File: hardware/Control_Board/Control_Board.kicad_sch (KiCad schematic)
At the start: 22 parts, among them J1 Left Motor, J2 Right Motor, J3 Battery, J4 MPU-6050, J5 Pitch Motor, Q1 2N3904, Q2 2N3904, Q4 2N3904, SW1 Extra_BTN, U1 ESP32-FREENOVE-WROVER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

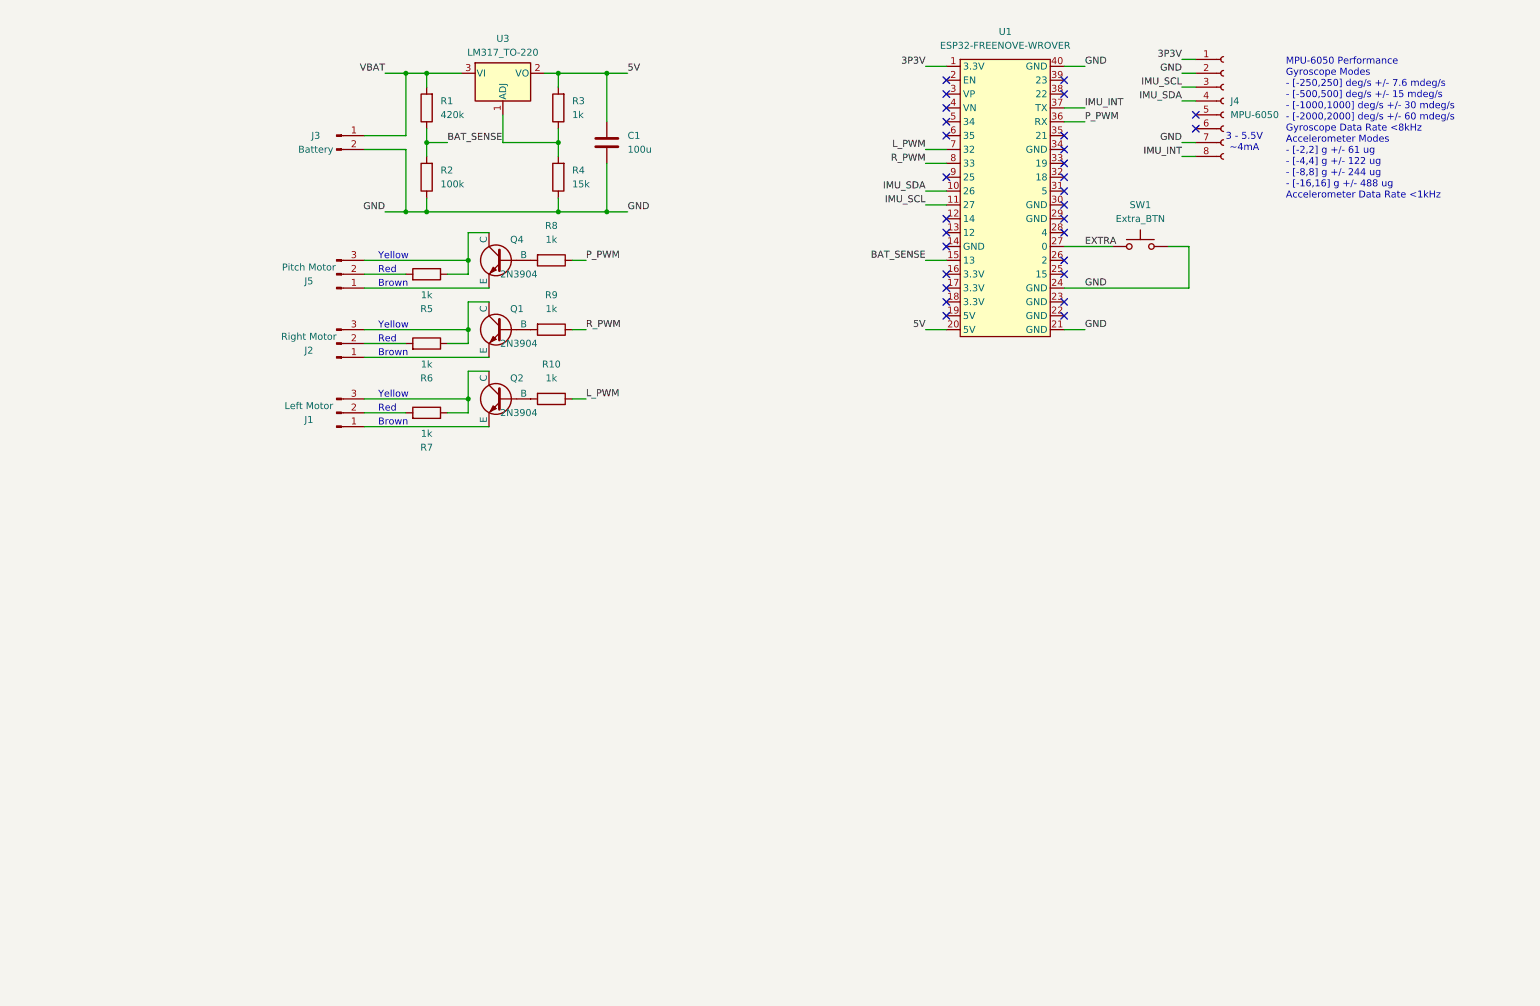
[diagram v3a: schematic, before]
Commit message: feat: upgraded imu code
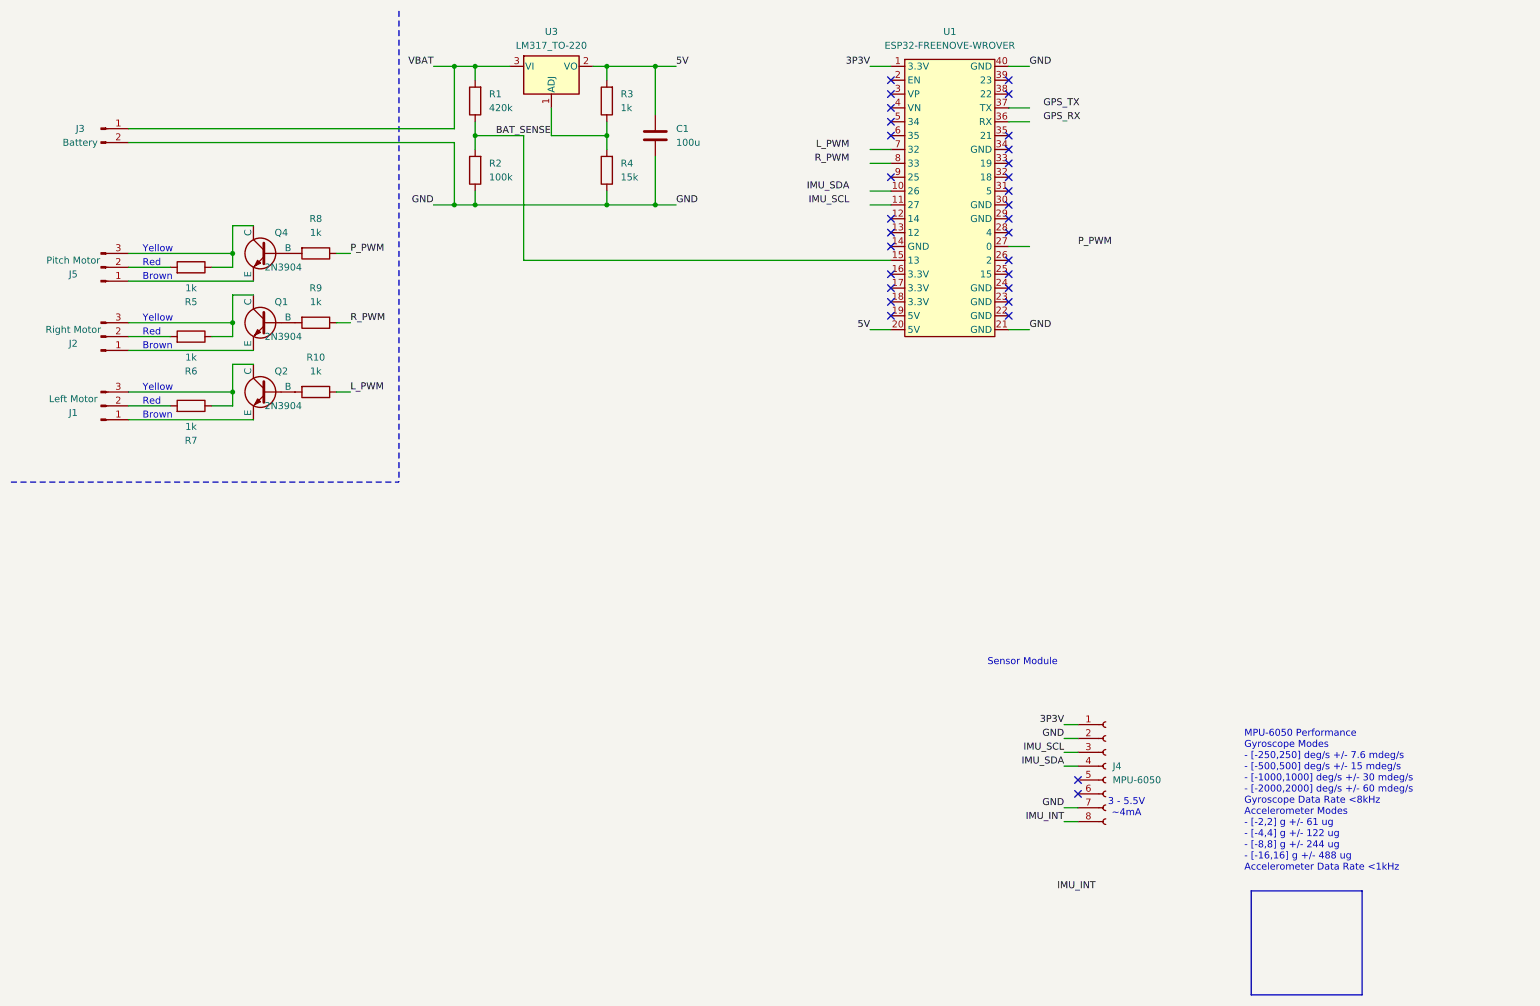
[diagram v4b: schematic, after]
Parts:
- removed SW1: Extra_BTN, symbol Switch:SW_Push
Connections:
- net GND: no longer U1.24 (GND)
- net IMU_INT: no longer U1.37 (TX)
- net IMU_SCL: no longer U1.11 (27)
- net IMU_SDA: no longer U1.10 (26)
- net L_PWM: no longer U1.7 (32)
- net P_PWM: no longer U1.36 (RX)
- net R_PWM: no longer U1.8 (33)
- net EXTRA: no longer names the net of U1.27 (0)
- no-connect marks 29 -> 30
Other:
- note added: "Sensor Module"
- moved on the sheet: C1, J1, J2, J3, J4, J5, Q1, Q2, Q4, R1, R10, R2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
